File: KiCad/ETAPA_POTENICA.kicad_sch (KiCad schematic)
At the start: 14 parts, among them U3 VNH5019A-E, U5 VNH5019A-E

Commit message: Versió final Esquematic
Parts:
- removed C_CP_DOOR2, C_VDD_DOOR3, C_WIN_1, C_WIN_CP1: 100nF, Capacitor_SMD:C_0805_2012Metric, symbol Device:C
- removed C_VDD_DOOR4: 10uF, Capacitor_SMD:CP_Elec_8x10, symbol Device:C
- removed C_WIN_2: 10uF, Capacitor_SMD:C_1206_3216Metric, symbol Device:C
- removed R_CS_DOOR2: 1k, Resistor_SMD:R_0805_2012Metric, symbol Device:R
- removed R_DIAGA_DOOR2, R_DIAGB_DOOR2, R_WIN_DIAGA1, R_WIN_DIAGB1: 3.3k, Resistor_SMD:R_0805_2012Metric, symbol Device:R
- removed R_WIN_CS1: 1,5K, Resistor_SMD:R_0805_2012Metric, symbol Device:R
- removed U3, U5: VNH5019A-E, Package_SO:ST_MultiPowerSO-30, symbol Driver_Motor:VNH5019A-E
- added C_CP_DOOR1, C_VDD_DOOR1, C_WIN_3, C_WIN_CP2: 100nF, Capacitor_SMD:C_0805_2012Metric, symbol Device:C
- added C_VDD_DOOR2: 10uF, Capacitor_SMD:CP_Elec_8x10, symbol Device:C
- added C_WIN_4: 10uF, Capacitor_SMD:C_1206_3216Metric, symbol Device:C
- added R_CS_DOOR1: 1k, Resistor_SMD:R_0805_2012Metric, symbol Device:R
- added R_DIAGA_DOOR1, R_DIAGB_DOOR1, R_WIN_DIAGA2, R_WIN_DIAGB2: 3.3k, Resistor_SMD:R_0805_2012Metric, symbol Device:R
- added R_WIN_CS2: 1,5K, Resistor_SMD:R_0805_2012Metric, symbol Device:R
- added U1, U2: VNH5019A-E, Package_SO:ST_MultiPowerSO-30, symbol Driver_Motor:VNH5019A-E
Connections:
- net +3.3V: now also R_DIAGA_DOOR1.2, R_DIAGB_DOOR1.2, R_WIN_DIAGA2.2, R_WIN_DIAGB2.2, U2.6 (CS_DIS)
- net DOOR_DIAGA: now also R_DIAGA_DOOR1.1, U2.5 (EN/DIAGA)
- net DOOR_DIAGB: now also R_DIAGB_DOOR1.1, U2.9 (EN/DIAGB)
- net DOOR_INA: now also U2.4 (INA)
- net DOOR_INB: now also U2.10 (INB)
- net DOOR_OUTA: now also U2.1 (OUTA), U2.25 (OUTA), U2.30 (OUTA), U2.33 (OUTA)
- net DOOR_OUTB: now also U2.15 (OUTB), U2.16 (OUTB), U2.21 (OUTB), U2.32 (OUTB)
- net DOOR_PWM: now also U2.7 (PWM)
- net GND: now also C_CP_DOOR1.1, C_VDD_DOOR1.2, C_VDD_DOOR2.2, C_WIN_3.2, C_WIN_4.2, C_WIN_CP2.1, R_CS_DOOR1.2, R_WIN_CS2.2, U1.6 (CS_DIS)
- net GNDPWR: now also U1.18 (GNDB), U1.19 (GNDB), U1.20 (GNDB), U1.26 (GNDA), U1.27 (GNDA), U1.28 (GNDA), U2.18 (GNDB), U2.19 (GNDB), U2.20 (GNDB), U2.26 (GNDA), U2.27 (GNDA), U2.28 (GNDA)
- net VBAT_PROT: now also C_VDD_DOOR1.1, C_VDD_DOOR2.1, C_WIN_3.1, C_WIN_4.1, U1.12 (VBAT), U1.13 (VCC), U1.23 (VCC), U1.3 (VCC), U1.31 (VCC), U2.12 (VBAT), U2.13 (VCC), U2.23 (VCC), U2.3 (VCC), U2.31 (VCC)
- net WIN_CURRENT_ADC: now also R_WIN_CS2.1, U1.8 (CS)
- net WIN_DIAGA: now also R_WIN_DIAGA2.1, U1.5 (EN/DIAGA)
- net WIN_DIAGB: now also R_WIN_DIAGB2.1, U1.9 (EN/DIAGB)
- net WIN_INA: now also U1.4 (INA)
- net WIN_INB: now also U1.10 (INB)
- net WIN_OUTA: now also U1.1 (OUTA), U1.25 (OUTA), U1.30 (OUTA), U1.33 (OUTA)
- net WIN_OUTB: now also U1.15 (OUTB), U1.16 (OUTB), U1.21 (OUTB), U1.32 (OUTB)
- net WIN_PWM: now also U1.7 (PWM)
- new net: C_WIN_CP2.2, U1.11 (CP)
- new net: R_CS_DOOR1.1, U2.8 (CS)
- new net: C_CP_DOOR1.2, U2.11 (CP)

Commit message: Versió final de l'esquematic
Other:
- note added: "MOTOR DE FINESTRA"
- note added: "MOTOR DE LA PORTA"
- moved on the sheet: C_CP_DOOR1, C_VDD_DOOR1, C_VDD_DOOR2, C_WIN_3, C_WIN_4, C_WIN_CP2, R_CS_DOOR1, R_DIAGA_DOOR1, R_DIAGB_DOOR1, R_WIN_CS2, R_WIN_DIAGA2, R_WIN_DIAGB2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

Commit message: 1ra versióPCB
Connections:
- net DOOR_OUTA renamed DOOR_MOTOR_A
- net DOOR_OUTB renamed DOOR_MOTOR_B
- net WIN_OUTA renamed WIN_MOTOR_A
- net WIN_OUTB renamed WIN_MOTOR_B
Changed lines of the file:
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@@
 		)
 	)
-	(hierarchical_label "WIN_OUTB"
+	(hierarchical_label "WIN_MOTOR_B"
 		(shape output)
 		(at 64.77 72.39 0)
@@
 		)
 	)
-	(hierarchical_label "DOOR_OUTB"
+	(hierarchical_label "DOOR_MOTOR_B"
 		(shape output)
 		(at 173.99 71.12 0)
@@
 		)
 	)
-	(hierarchical_label "DOOR_OUTA"
+	(hierarchical_label "DOOR_MOTOR_A"
 		(shape output)
 		(at 173.99 68.58 0)
@@
 		)
 	)
-	(hierarchical_label "WIN_OUTA"
+	(hierarchical_label "WIN_MOTOR_A"
 		(shape output)
 		(at 64.77 69.85 0)

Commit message: Versió de placement PCB
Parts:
- C_VDD_DOOR2: footprint Capacitor_SMD:CP_Elec_8x10 -> Capacitor_SMD:C_1206_3216Metric
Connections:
- net GND: no longer C_CP_DOOR1.1, C_VDD_DOOR1.2, C_VDD_DOOR2.2, C_WIN_3.2, C_WIN_4.2, C_WIN_CP2.1, R_CS_DOOR1.2, R_WIN_CS2.2
- net GNDPWR: now also C_CP_DOOR1.1, C_VDD_DOOR1.2, C_VDD_DOOR2.2, C_WIN_3.2, C_WIN_4.2, C_WIN_CP2.1, R_CS_DOOR1.2, R_WIN_CS2.2

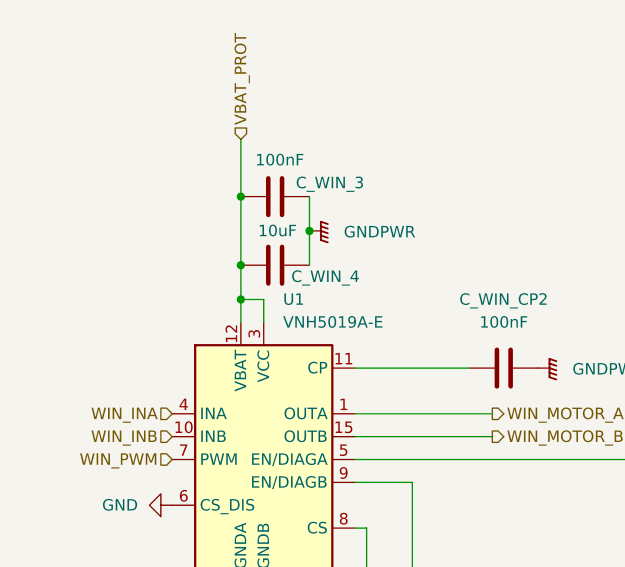
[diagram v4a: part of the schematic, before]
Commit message: Bus CAN i USART
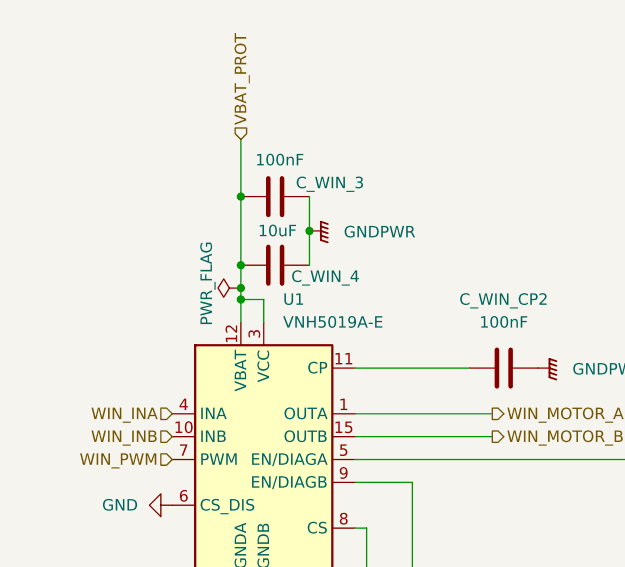
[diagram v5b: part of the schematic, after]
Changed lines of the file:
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@@
+	)
+	(junction
+		(at 36.83 55.88)
+		(diameter 0)
+		(color 0 0 0 0)
 	)
 	(junction
@@
 	(wire
 		(pts
-			(xy 36.83 53.34) (xy 36.83 57.15)
+			(xy 36.83 53.34) (xy 36.83 55.88)
 		)
 		(stroke
@@
 		(pts
 			(xy 134.62 78.74) (xy 137.16 78.74)
+		)
+		(stroke
+			(width 0)
+			(type default)
+		)
+	)
+	(wire
+		(pts
+			(xy 36.83 55.88) (xy 36.83 57.15)
 		)
 		(stroke
@@
 					(unit 1)
 				)
+			)
+		)
+	)
+	(symbol
+		(lib_id "power:PWR_FLAG")
+		(at 36.83 55.88 90)
+		(unit 1)
+		(exclude_from_sim no)
+		(in_bom yes)
+		(on_board yes)
+		(dnp no)
+		(property "Reference" "#FLG05"
+			(at 34.925 55.88 0)
+			(effects
+				(font
+					(size 1.27 1.27)
+				)
+				(hide yes)
+			)
+		)
+		(property "Value" "PWR_FLAG"
+			(at 33.02 55.372 0)
+			(effects
+				(font
+					(size 1.27 1.27)
+				)
+			)
+		)
+		(property "Footprint" ""
+			(at 36.83 55.88 0)
+			(effects
+				(font
+					(size 1.27 1.27)
+				)
+				(hide yes)
+			)
+		)
+		(property "Datasheet" "~"
+			(at 36.83 55.88 0)
+			(effects
+				(font
+					(size 1.27 1.27)
+				)
+				(hide yes)
+			)
+		)
+		(property "Description" "Special symbol for telling ERC where power comes from"
+			(at 36.83 55.88 0)
+			(effects
+				(font
+					(size 1.27 1.27)
+				)
+				(hide yes)
+			)
+		)
+		(pin "1"
+		)
+		(instances
+			(project "PROJECTE_EINES"
+				(path "/347831db-5db9-4aff-ad32-e56fd770e219/0182dfdd-06e0-4cd2-9407-e3ad60659aa3"
+					(reference "#FLG05")
+					(unit 1)
+				)

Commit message: Errors solucionats
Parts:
- renumbered C_WIN_3 to C_WIN_1, C_WIN_4 to C_WIN_2, C_WIN_CP2 to C_WIN_CP1, R_WIN_CS2 to R_WIN_CS1, R_WIN_DIAGA2 to R_WIN_DIAGA1, R_WIN_DIAGB2 to R_WIN_DIAGB1, U1 to U3, U2 to U5
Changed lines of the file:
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@@
 		(on_board yes)
 		(dnp no)
-		(property "Reference" "#PWR041"
+		(property "Reference" "#PWR034"
 			(at 134.62 82.55 0)
 			(effects
@@
 			(project "PROJECTE_EINES"
 				(path "/347831db-5db9-4aff-ad32-e56fd770e219/0182dfdd-06e0-4cd2-9407-e3ad60659aa3"
-					(reference "#PWR041")
+					(reference "#PWR034")
 					(unit 1)
 				)
@@
 		(on_board yes)
 		(dnp no)
-		(property "Reference" "#FLG05"
+		(property "Reference" "#FLG04"
 			(at 34.925 55.88 0)
 			(effects
@@
 			(project "PROJECTE_EINES"
 				(path "/347831db-5db9-4aff-ad32-e56fd770e219/0182dfdd-06e0-4cd2-9407-e3ad60659aa3"
-					(reference "#FLG05")
+					(reference "#FLG04")
 					(unit 1)
 				)
@@
 		(dnp no)
 		(fields_autoplaced yes)
-		(property "Reference" "#PWR042"
+		(property "Reference" "#PWR035"
 			(at 146.05 97.79 0)
 			(effects
@@
 			(project "PROJECTE_EINES"
 				(path "/347831db-5db9-4aff-ad32-e56fd770e219/0182dfdd-06e0-4cd2-9407-e3ad60659aa3"
-					(reference "#PWR042")
+					(reference "#PWR035")
 					(unit 1)
 				)
@@
 		(dnp no)
 		(fields_autoplaced yes)
-		(property "Reference" "#PWR08"
+		(property "Reference" "#PWR031"
 			(at 74.93 64.77 0)
 			(effects
@@
 			(project "PROJECTE_EINES"
 				(path "/347831db-5db9-4aff-ad32-e56fd770e219/0182dfdd-06e0-4cd2-9407-e3ad60659aa3"
-					(reference "#PWR08")
+					(reference "#PWR031")
 					(unit 1)
 				)
@@
 		(dnp no)
 		(fields_autoplaced yes)
-		(property "Reference" "#PWR07"
+		(property "Reference" "#PWR028"
 			(at 38.1 102.87 0)
 			(effects
@@
 			(project "PROJECTE_EINES"
 				(path "/347831db-5db9-4aff-ad32-e56fd770e219/0182dfdd-06e0-4cd2-9407-e3ad60659aa3"
-					(reference "#PWR07")
+					(reference "#PWR028")
 					(unit 1)
 				)
@@
 		(dnp no)
 		(fields_autoplaced yes)
-		(property "Reference" "C_WIN_CP2"
+		(property "Reference" "C_WIN_CP1"
 			(at 66.04 57.15 90)
 			(effects
@@
 			(project "PROJECTE_EINES"
 				(path "/347831db-5db9-4aff-ad32-e56fd770e219/0182dfdd-06e0-4cd2-9407-e3ad60659aa3"
-					(reference "C_WIN_CP2")
+					(reference "C_WIN_CP1")
 					(unit 1)
 				)
@@
 		(on_board yes)
 		(dnp no)
-		(property "Reference" "#PWR060"
+		(property "Reference" "#PWR039"
 			(at 173.99 81.28 0)
 			(effects
@@
 			(project "PROJECTE_EINES"
 				(path "/347831db-5db9-4aff-ad32-e56fd770e219/0182dfdd-06e0-4cd2-9407-e3ad60659aa3"
-					(reference "#PWR060")
+					(reference "#PWR039")
 					(unit 1)
 				)
@@
 		(on_board yes)
 		(dnp no)
-		(property "Reference" "#PWR062"
+		(property "Reference" "#PWR042"
 			(at 200.66 67.31 0)
 			(effects
@@
 			(project "PROJECTE_EINES"
 				(path "/347831db-5db9-4aff-ad32-e56fd770e219/0182dfdd-06e0-4cd2-9407-e3ad60659aa3"
-					(reference "#PWR062")
+					(reference "#PWR042")
 					(unit 1)
 				)
@@
 		(on_board yes)
 		(dnp no)
-		(property "Reference" "R_WIN_DIAGB2"
+		(property "Reference" "R_WIN_DIAGB1"
 			(at 93.726 84.074 90)
 			(effects
@@
 			(project "PROJECTE_EINES"
 				(path "/347831db-5db9-4aff-ad32-e56fd770e219/0182dfdd-06e0-4cd2-9407-e3ad60659aa3"
-					(reference "R_WIN_DIAGB2")
+					(reference "R_WIN_DIAGB1")
 					(unit 1)
 				)
@@
 		(dnp no)
 		(fields_autoplaced yes)
-		(property "Reference" "#PWR021"
+		(property "Reference" "#PWR030"
 			(at 50.8 107.95 0)
 			(effects
@@
 			(project "PROJECTE_EINES"
 				(path "/347831db-5db9-4aff-ad32-e56fd770e219/0182dfdd-06e0-4cd2-9407-e3ad60659aa3"
-					(reference "#PWR021")
+					(reference "#PWR030")
 					(unit 1)
 				)
@@
 		(dnp no)
 		(fields_autoplaced yes)
-		(property "Reference" "#PWR031"
+		(property "Reference" "#PWR041"
 			(at 182.88 68.58 0)
 			(effects
@@
 			(project ""
 				(path "/347831db-5db9-4aff-ad32-e56fd770e219/0182dfdd-06e0-4cd2-9407-e3ad60659aa3"
-					(reference "#PWR031")
+					(reference "#PWR041")
 					(unit 1)
 				)
@@
 		(on_board yes)
 		(dnp no)
-		(property "Reference" "C_WIN_3"
+		(property "Reference" "C_WIN_1"
 			(at 46.736 44.196 90)
 			(effects
@@
 			(project "PROJECTE_EINES"
 				(path "/347831db-5db9-4aff-ad32-e56fd770e219/0182dfdd-06e0-4cd2-9407-e3ad60659aa3"
-					(reference "C_WIN_3")
+					(reference "C_WIN_1")
 					(unit 1)
 				)
@@
 		(on_board yes)
 		(dnp no)
-		(property "Reference" "R_WIN_DIAGA2"
+		(property "Reference" "R_WIN_DIAGA1"
 			(at 94.488 66.802 90)
 			(effects
@@
 			(project "PROJECTE_EINES"
 				(path "/347831db-5db9-4aff-ad32-e56fd770e219/0182dfdd-06e0-4cd2-9407-e3ad60659aa3"
-					(reference "R_WIN_DIAGA2")
+					(reference "R_WIN_DIAGA1")
 					(unit 1)
 				)
@@
 		(dnp no)
 		(fields_autoplaced yes)
-		(property "Reference" "#PWR020"
+		(property "Reference" "#PWR029"
 			(at 49.53 49.53 0)
 			(effects
@@
 			(project ""
 				(path "/347831db-5db9-4aff-ad32-e56fd770e219/0182dfdd-06e0-4cd2-9407-e3ad60659aa3"
-					(reference "#PWR020")
+					(reference "#PWR029")
 					(unit 1)
 				)
@@
 		(dnp no)
 		(fields_autoplaced yes)
-		(property "Reference" "#PWR032"
+		(property "Reference" "#PWR036"
 			(at 157.48 48.26 0)
 			(effects
@@
 			(project ""
 				(path "/347831db-5db9-4aff-ad32-e56fd770e219/0182dfdd-06e0-4cd2-9407-e3ad60659aa3"
-					(reference "#PWR032")
+					(reference "#PWR036")
 					(unit 1)
 				)
@@
 		(on_board yes)
 		(dnp no)
-		(property "Reference" "#PWR039"
+		(property "Reference" "#PWR032"
 			(at 90.17 83.82 0)
 			(effects
@@
 			(project "PROJECTE_EINES"
 				(path "/347831db-5db9-4aff-ad32-e56fd770e219/0182dfdd-06e0-4cd2-9407-e3ad60659aa3"
-					(reference "#PWR039")
+					(reference "#PWR032")
 					(unit 1)
 				)
@@
 		(on_board yes)
 		(dnp no)
-		(property "Reference" "#PWR040"
+		(property "Reference" "#PWR033"
 			(at 91.44 64.77 0)
 			(effects
@@
 			(project "PROJECTE_EINES"
 				(path "/347831db-5db9-4aff-ad32-e56fd770e219/0182dfdd-06e0-4cd2-9407-e3ad60659aa3"
-					(reference "#PWR040")
+					(reference "#PWR033")
 					(unit 1)
 				)
@@
 		(dnp no)
 		(fields_autoplaced yes)
-		(property "Reference" "#PWR06"
+		(property "Reference" "#PWR027"
 			(at 22.86 80.01 0)
 			(effects
@@
 			(project "PROJECTE_EINES"
 				(path "/347831db-5db9-4aff-ad32-e56fd770e219/0182dfdd-06e0-4cd2-9407-e3ad60659aa3"
-					(reference "#PWR06")
+					(reference "#PWR027")
 					(unit 1)
 				)
@@
 		(dnp no)
 		(fields_autoplaced yes)
-		(property "Reference" "#PWR030"
+		(property "Reference" "#PWR038"
 			(at 170.18 99.06 0)
 			(effects
@@
 			(project ""
 				(path "/347831db-5db9-4aff-ad32-e56fd770e219/0182dfdd-06e0-4cd2-9407-e3ad60659aa3"
-					(reference "#PWR030")
+					(reference "#PWR038")
 					(unit 1)
 				)
@@
 		(on_board yes)
 		(dnp no)
-		(property "Reference" "C_WIN_4"
+		(property "Reference" "C_WIN_2"
 			(at 46.228 54.61 90)
 			(effects
@@
 			(project "PROJECTE_EINES"
 				(path "/347831db-5db9-4aff-ad32-e56fd770e219/0182dfdd-06e0-4cd2-9407-e3ad60659aa3"
-					(reference "C_WIN_4")
+					(reference "C_WIN_2")
 					(unit 1)
 				)
@@
 		(dnp no)
 		(fields_autoplaced yes)
-		(property "Reference" "U2"
+		(property "Reference" "U5"
 			(at 149.4633 55.88 0)
 			(effects
@@
 			(project "PROJECTE_EINES"
 				(path "/347831db-5db9-4aff-ad32-e56fd770e219/0182dfdd-06e0-4cd2-9407-e3ad60659aa3"
-					(reference "U2")
+					(reference "U5")
 					(unit 1)
 				)
@@
 		(dnp no)
 		(fields_autoplaced yes)
-		(property "Reference" "R_WIN_CS2"
+		(property "Reference" "R_WIN_CS1"
 			(at 53.34 99.0599 0)
 			(effects
@@
 			(project "PROJECTE_EINES"
 				(path "/347831db-5db9-4aff-ad32-e56fd770e219/0182dfdd-06e0-4cd2-9407-e3ad60659aa3"
-					(reference "R_WIN_CS2")
+					(reference "R_WIN_CS1")
 					(unit 1)
 				)
@@
 		(dnp no)
 		(fields_autoplaced yes)
-		(property "Reference" "U1"
+		(property "Reference" "U3"
 			(at 41.5133 57.15 0)
 			(effects
@@
 			(project "PROJECTE_EINES"
 				(path "/347831db-5db9-4aff-ad32-e56fd770e219/0182dfdd-06e0-4cd2-9407-e3ad60659aa3"
-					(reference "U1")
-					(unit 1)
-				)
+					(reference "U3")
+					(unit 1)
+				)
